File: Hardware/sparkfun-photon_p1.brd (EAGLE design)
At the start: 68.6 x 53.3 mm, 44 parts, among them U1 WM-N-BM-14

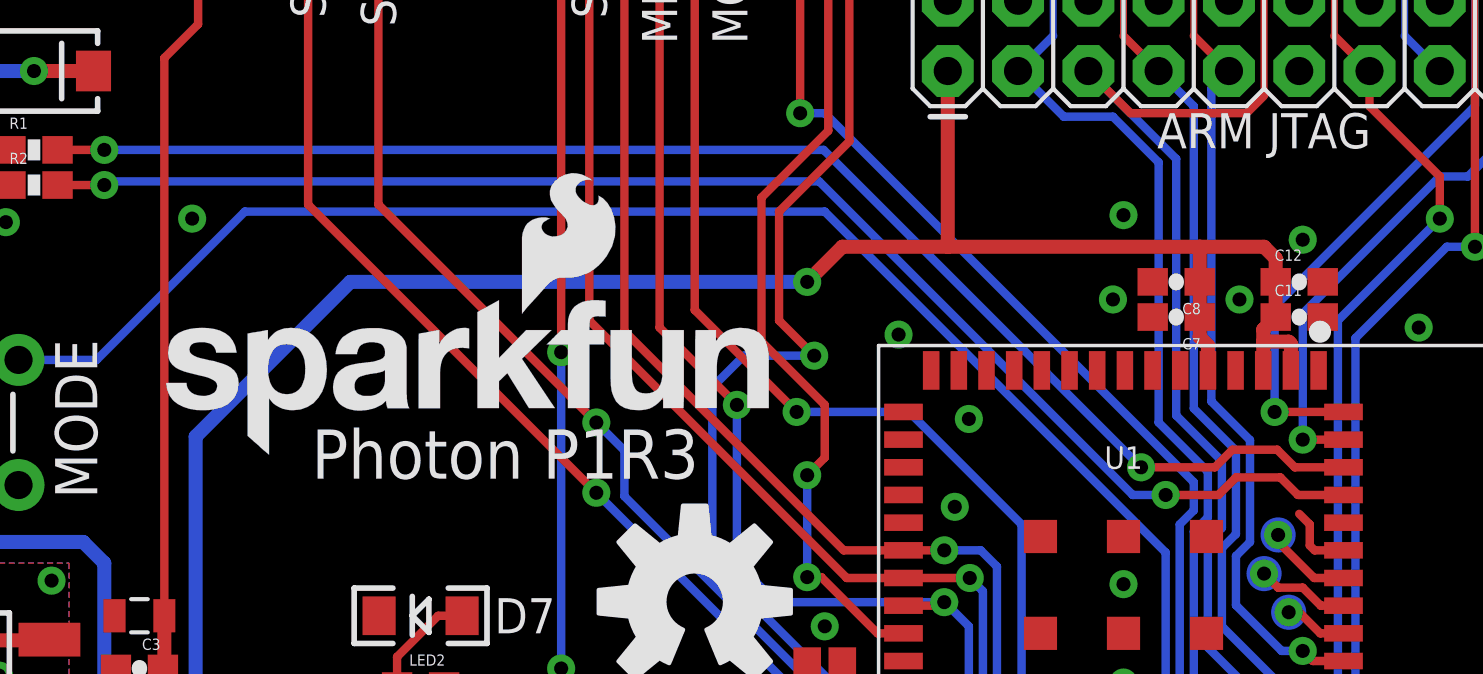
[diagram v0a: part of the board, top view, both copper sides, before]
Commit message: Adding PROD_ID to USB connector.
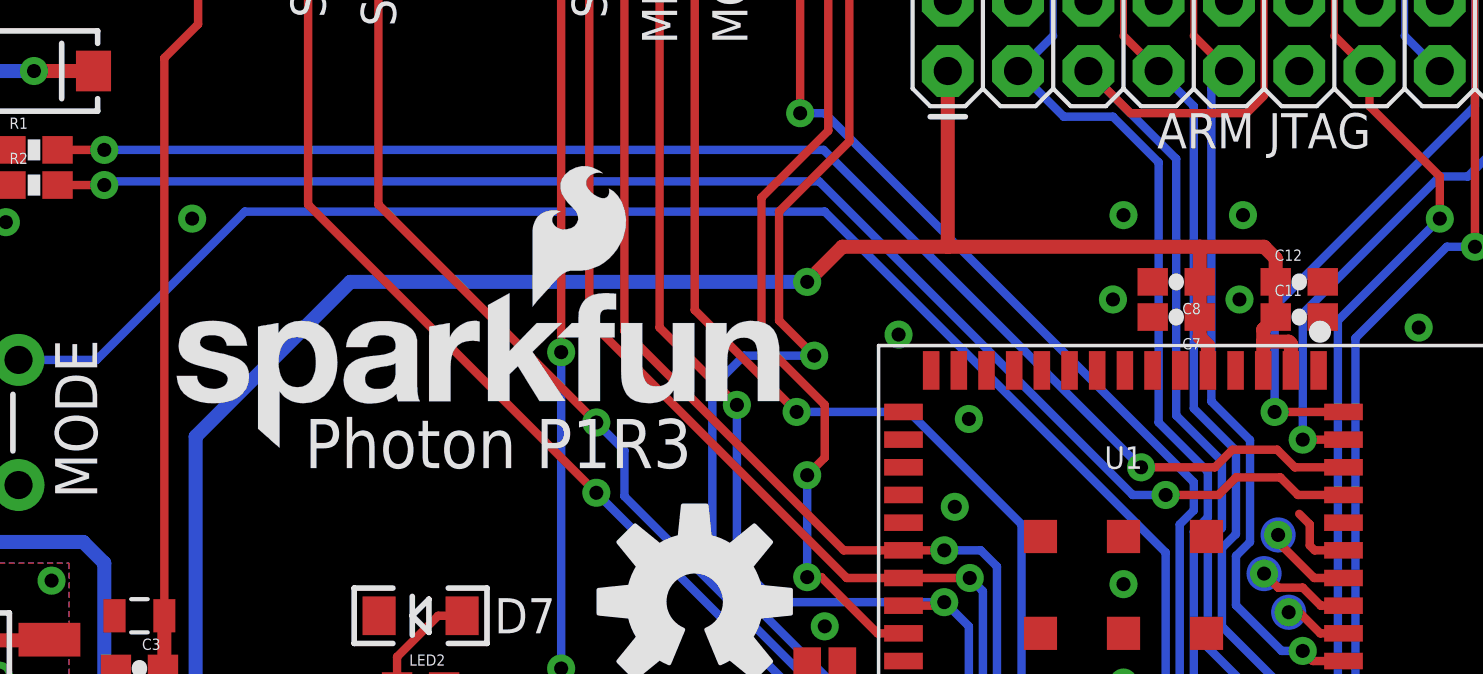
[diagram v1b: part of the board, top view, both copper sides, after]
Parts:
- moved LOGO2 0.46 mm to (13.3, 28.2)
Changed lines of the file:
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@@
 <layer number="39" name="tKeepout" color="4" fill="11" visible="no" active="yes"/>
 <layer number="40" name="bKeepout" color="1" fill="11" visible="no" active="yes"/>
-<layer number="41" name="tRestrict" color="4" fill="10" visible="yes" active="yes"/>
+<layer number="41" name="tRestrict" color="4" fill="10" visible="no" active="yes"/>
 <layer number="42" name="bRestrict" color="1" fill="10" visible="no" active="yes"/>
 <layer number="43" name="vRestrict" color="2" fill="10" visible="no" active="yes"/>
@@
 <layer number="47" name="Measures" color="7" fill="1" visible="no" active="yes"/>
 <layer number="48" name="Document" color="7" fill="1" visible="no" active="yes"/>
-<layer number="49" name="Reference" color="7" fill="1" visible="no" active="yes"/>
+<layer number="49" name="Reference" color="7" fill="1" visible="yes" active="yes"/>
 <layer number="50" name="dxf" color="7" fill="1" visible="no" active="no"/>
 <layer number="51" name="tDocu" color="6" fill="1" visible="yes" active="yes"/>
@@
 <text x="25.527" y="22.225" size="1.27" layer="21" font="vector" ratio="15" align="center-left">D7</text>
 <text x="25.527" y="10.795" size="1.27" layer="21" font="vector" ratio="15" align="center-left">POWER</text>
-<text x="18.923" y="28.067" size="1.778" layer="21" font="vector" ratio="15" align="center-left">Photon P1R3</text>
+<text x="18.669" y="28.448" size="1.778" layer="21" font="vector" ratio="15" align="center-left">Photon P1R3</text>
 <text x="9.652" y="29.337" size="1.524" layer="21" font="vector" ratio="15" rot="R90" align="top-center">MODE</text>
 <text x="9.652" y="48.387" size="1.524" layer="21" font="vector" ratio="15" rot="R90" align="top-center">RESET</text>
@@
 <attribute name="PROD_ID" value="CAP-00810" x="54.61" y="34.29" size="1.778" layer="27" font="vector" ratio="15" display="off"/>
 </element>
-<element name="LOGO2" library="SparkFun-Aesthetics" package="SFE_LOGO_NAME_FLAME_.2" value="SFE_LOGO_NAME_FLAME.2_INCH" x="12.954" y="27.94"/>
+<element name="LOGO2" library="SparkFun-Aesthetics" package="SFE_LOGO_NAME_FLAME_.2" value="SFE_LOGO_NAME_FLAME.2_INCH" x="13.335" y="28.194"/>
 <element name="LOGO1" library="SparkFun-Aesthetics" package="OSHW-LOGO-L" value="OSHW-LOGOL" x="32.766" y="22.733"/>
 <element name="U1" library="sparkfun_photon_temp" package="WM-N-BM-14" value="WM-N-BM-14" x="48.26" y="21.59">
@@
 <via x="40.132" y="32.385" extent="1-16" drill="0.508"/>
 <via x="47.879" y="33.655" extent="1-16" drill="0.508"/>
-<via x="54.737" y="35.814" extent="1-16" drill="0.508"/>
+<via x="52.578" y="36.703" extent="1-16" drill="0.508"/>
 <via x="58.928" y="32.639" extent="1-16" drill="0.508"/>
 <via x="43.18" y="8.763" extent="1-16" drill="0.508"/>

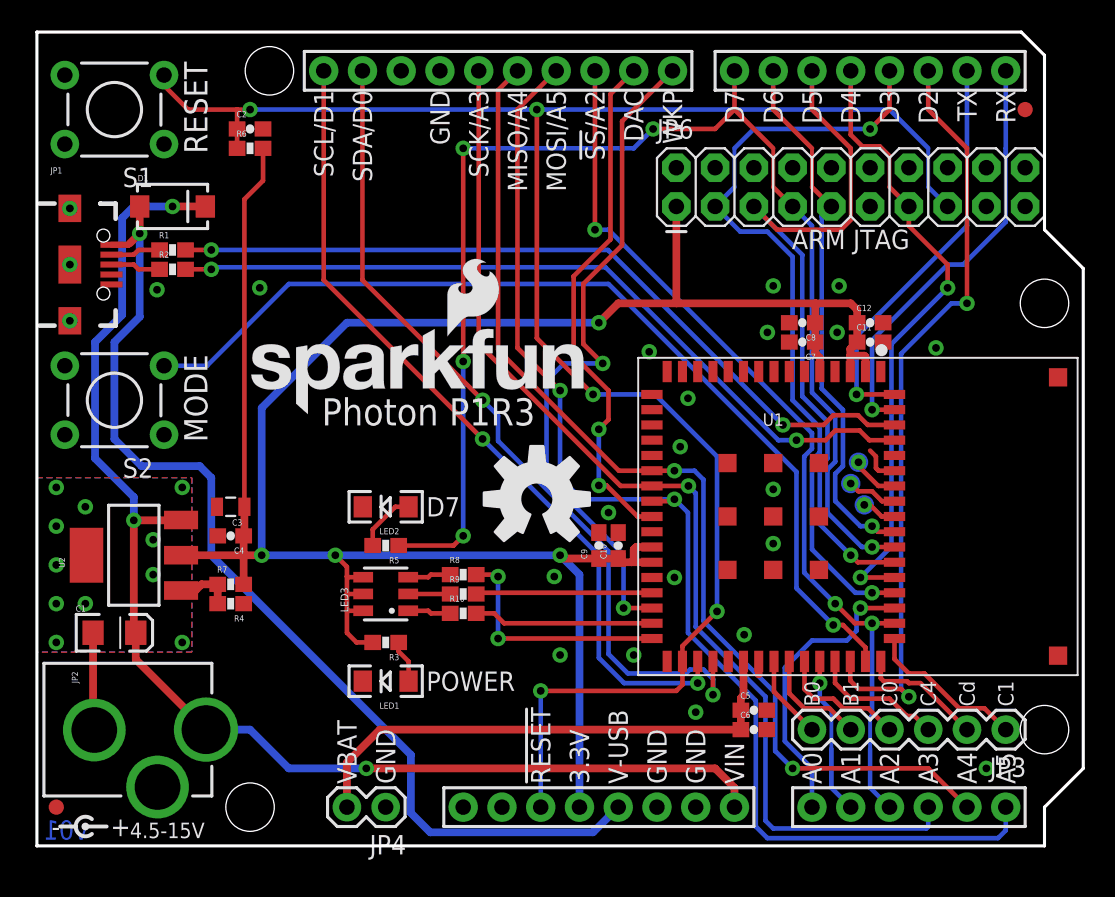
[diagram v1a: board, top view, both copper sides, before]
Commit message: Added measurements. Re-routed corner pins, moved JP3 away from standoff.
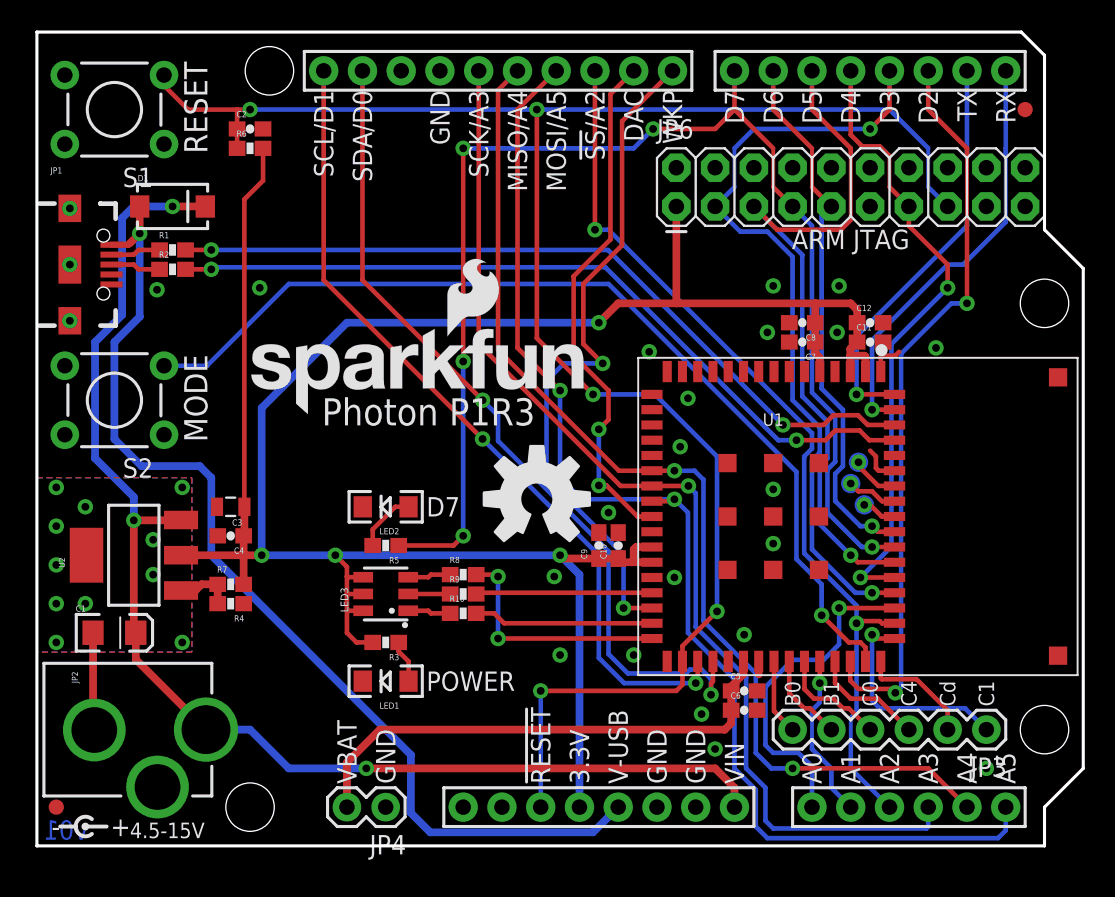
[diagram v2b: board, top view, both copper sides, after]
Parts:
- moved FRAME1 2.54 mm to (15.2, -11.4)
- moved C6 1.42 mm to (46.4, 8.89)
- moved C5 1.42 mm to (46.4, 10.2)
- moved JP3 1.27 mm to (62.2, 7.62)
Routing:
- net PC1: track 10.6 -> 14.2 mm, vias 0 -> 1
- net GND: track 9.86 -> 13.1 mm, vias 23 -> 24
- net A0: track 19.4 -> 22.1 mm
- net D2: track 50.2 -> 48.9 mm
- net PC0: track 8.49 -> 7.22 mm
- net PB1: track 7.11 -> 5.84 mm
- net PC4: track 8.79 -> 7.52 mm
- net A4: track 69.6 -> 70.4 mm
- net A2: track 59.4 -> 60.1 mm, vias 3 -> 2
- net VBAT: track 34.2 -> 33.6 mm
- net PC13: track 8.15 -> 7.62 mm
- net PB0: track 5.50 -> 4.98 mm

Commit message: Moving silk indicator on P1. Labeling RGB LED. Re-routing some grounds.
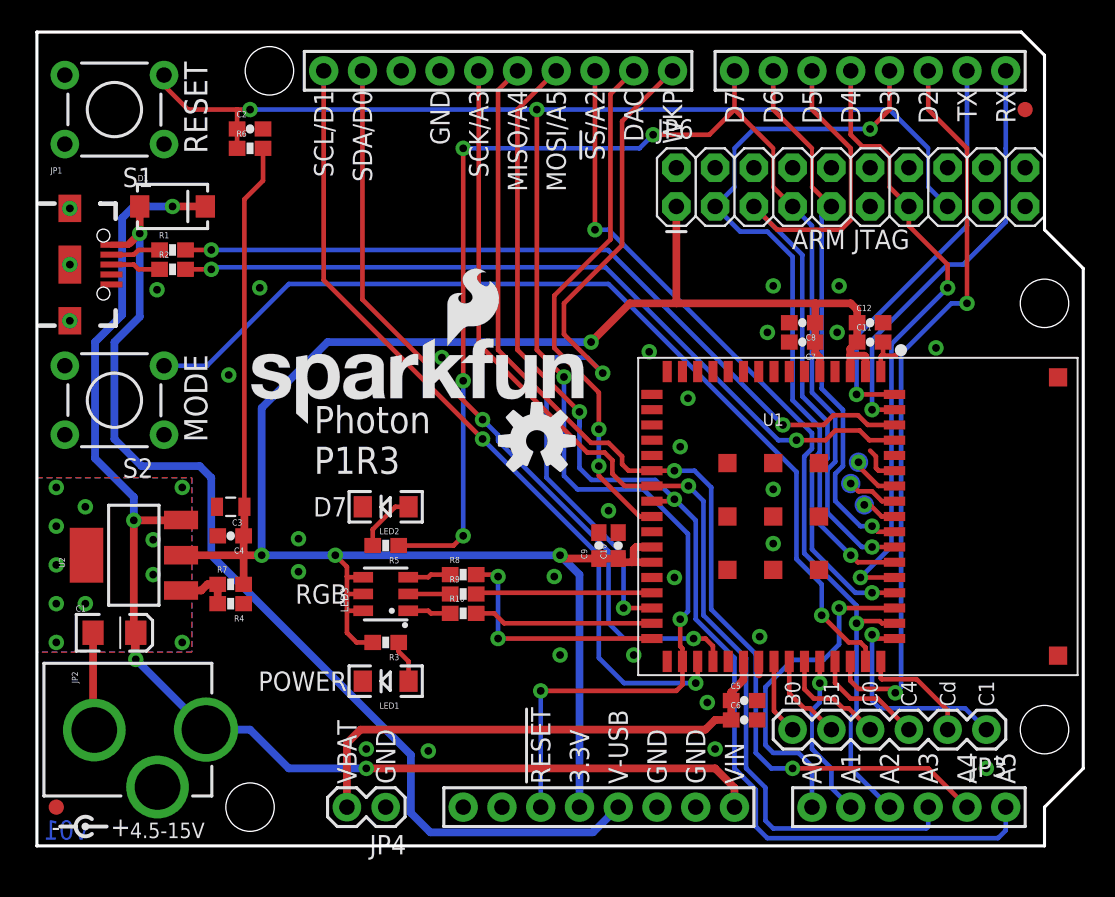
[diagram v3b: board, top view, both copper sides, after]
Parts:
- LOGO1: value OSHW-LOGOL -> OSHW-LOGOM; device SparkFun-Aesthetics:OSHW-LOGO-L -> SparkFun-Aesthetics:OSHW-LOGO-M
- moved LOGO1 3.81 mm to (32.8, 26.5)
- moved C5 0.63 mm to (46.4, 9.53)
- moved C6 0.63 mm to (46.4, 8.26)
- moved LOGO2 0.63 mm to (13.3, 27.6)
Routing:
- net D0: track 55.8 -> 51.4 mm
- net WKP: track 45.1 -> 47.9 mm
- net VIN: track 83.6 -> 85.5 mm, vias 3 -> 4
- net !RST: track 122.3 -> 121.0 mm
- net VBAT: track 33.6 -> 34.2 mm
- net A3: track 71.7 -> 72.3 mm
- net GND: vias 24 -> 30
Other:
- board text added: "RGB"
